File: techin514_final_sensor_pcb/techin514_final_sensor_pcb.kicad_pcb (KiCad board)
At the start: 2 copper layers, 7 parts, among them J2 J_BAT, J4 J_LDO, J6 J_IMU, J7 J_PWR

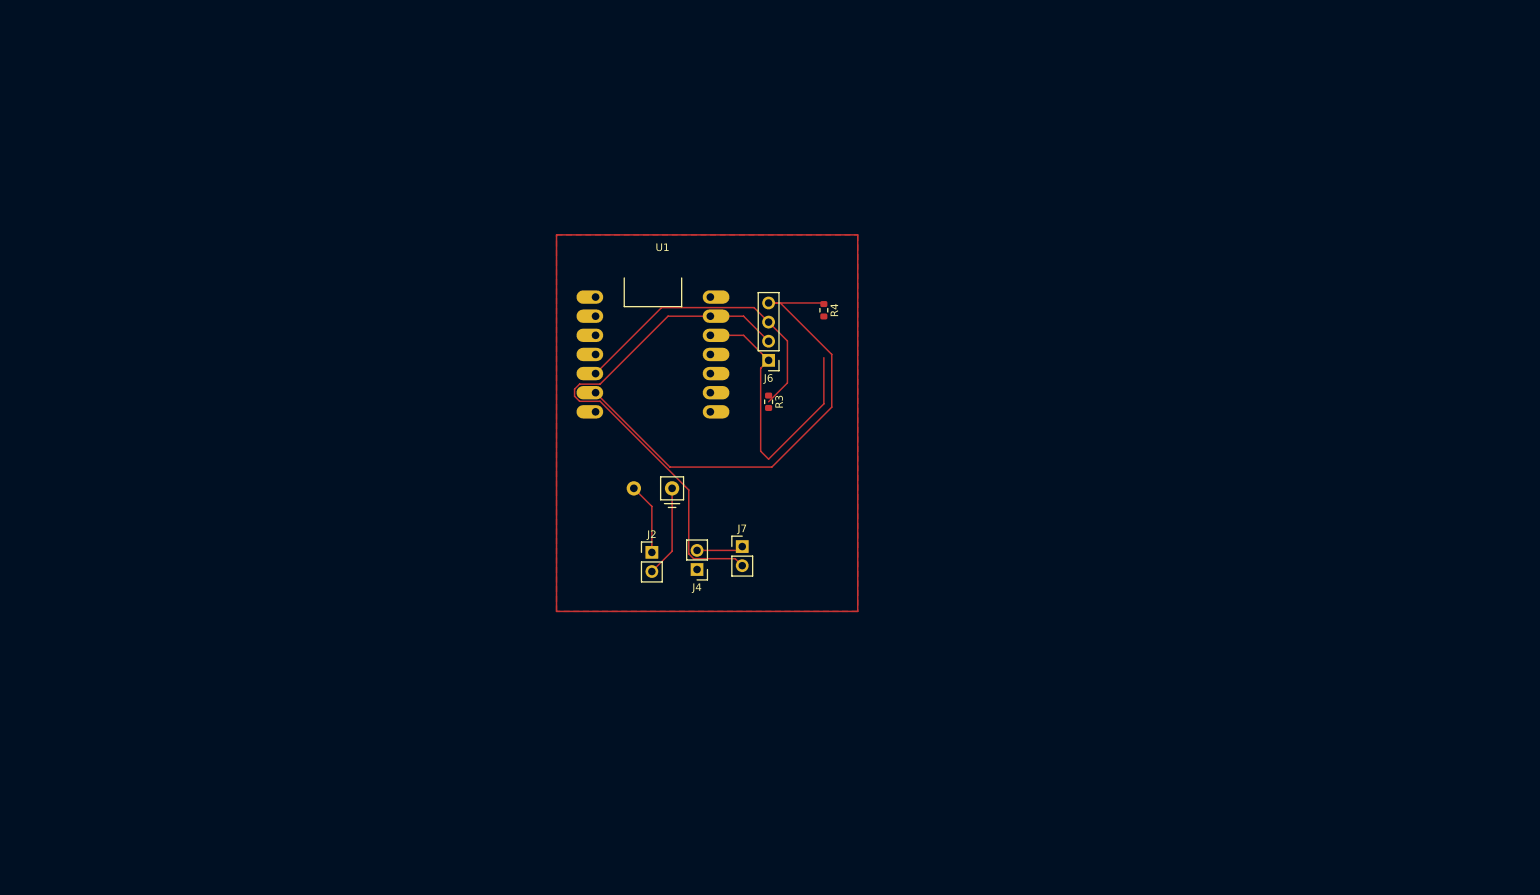
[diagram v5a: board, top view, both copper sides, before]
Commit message: update ble
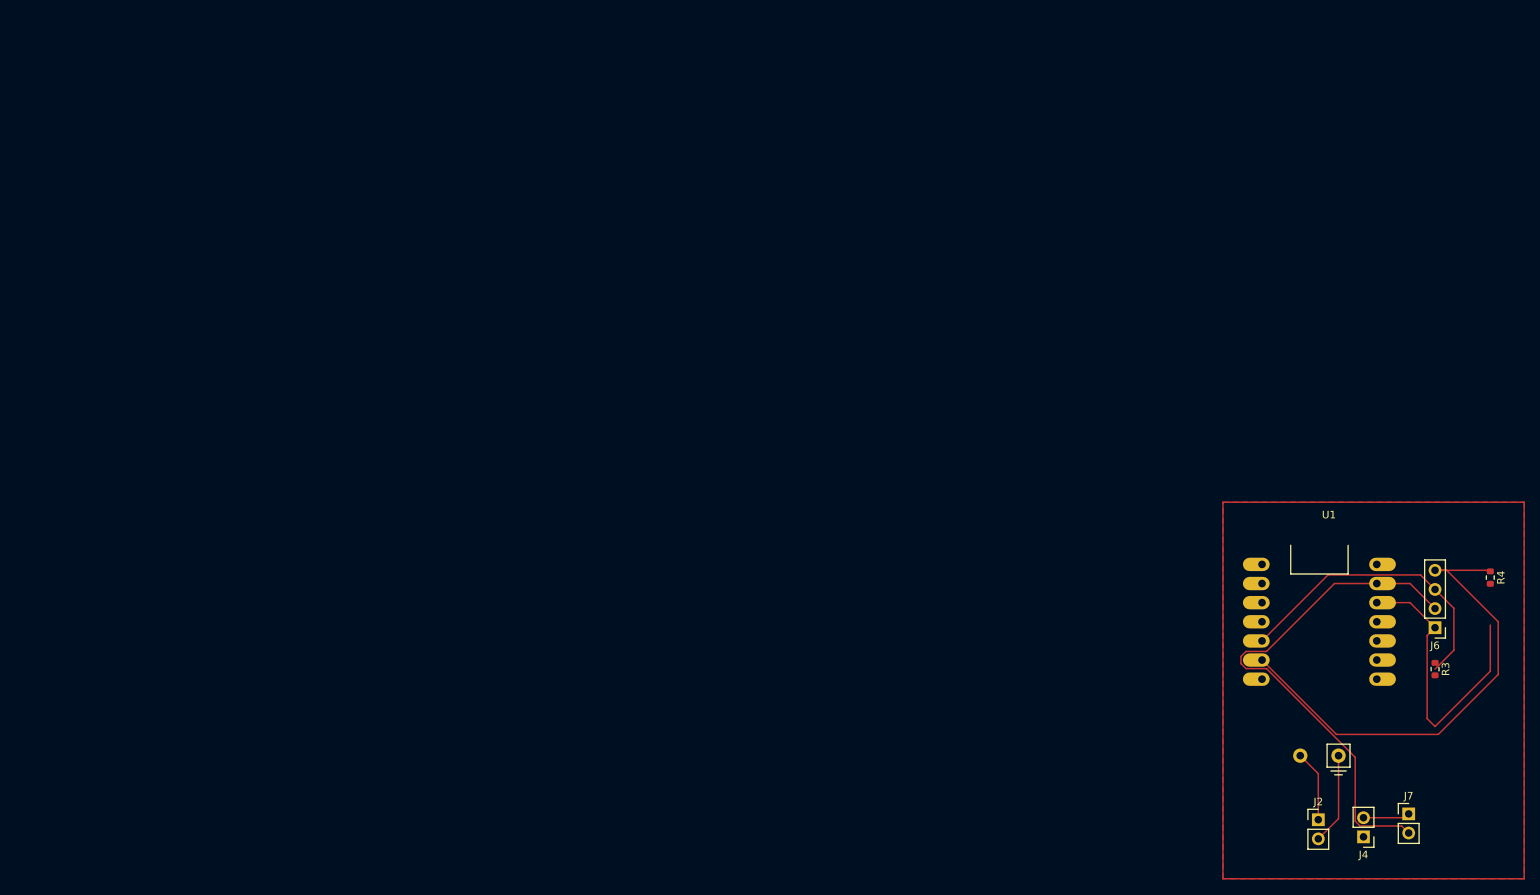
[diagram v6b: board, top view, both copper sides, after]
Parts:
- moved J2 95.4 mm to (223.1, 151.3)
- moved J4 95.4 mm to (229.1, 153.6)
- moved J6 95.4 mm to (238.6, 125.8)
- moved J7 95.4 mm to (235.1, 150.6)
- moved R3 95.4 mm to (238.6, 131.3)
- moved R4 95.4 mm to (245.9, 119.2)
- moved U1 95.4 mm to (223.2, 125.0)
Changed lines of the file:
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@@
 	(paper "A4")
 	(title_block
-		(title "Pet Activity & Proximity Tracker")
+		(title "Pet Activity & Proximity Tracker(Sensor PCB)")
 		(date "2026-02-04")
 		(rev "v0.1(draft)")
@@
 	(footprint "Connector_PinHeader_2.54mm:PinHeader_1x02_P2.54mm_Vertical"
 		(layer "F.Cu")
-		(at 140.564661 118.104 180)
+		(at 229.064661 153.604 180)
 		(descr "Through hole straight pin header, 1x02, 2.54mm pitch, single row")
 		(tags "Through hole pin header THT 1x02 2.54mm single row")
@@
 	(footprint "Connector_PinHeader_2.54mm:PinHeader_1x02_P2.54mm_Vertical"
 		(layer "F.Cu")
-		(at 146.564661 115.054)
+		(at 235.064661 150.554)
 		(descr "Through hole straight pin header, 1x02, 2.54mm pitch, single row")
 		(tags "Through hole pin header THT 1x02 2.54mm single row")
@@
 	(footprint "Resistor_SMD:R_0603_1608Metric"
 		(layer "F.Cu")
-		(at 157.402161 83.675 -90)
+		(at 245.902161 119.175 -90)
 		(descr "Resistor SMD 0603 (1608 Metric), square (rectangular) end terminal, IPC-7351 nominal, (Body size source: IPC-SM-782 page 72, https://www.pcb-3d.com/wordpress/wp-content/uploads/ipc-sm-782a_amendment_1_and_2.pdf), generated with kicad-footprint-generator")
 		(tags "resistor")
@@
 	(footprint "Resistor_SMD:R_0603_1608Metric"
 		(layer "F.Cu")
-		(at 150.064661 95.829 -90)
+		(at 238.564661 131.329 -90)
 		(descr "Resistor SMD 0603 (1608 Metric), square (rectangular) end terminal, IPC-7351 nominal, (Body size source: IPC-SM-782 page 72, https://www.pcb-3d.com/wordpress/wp-content/uploads/ipc-sm-782a_amendment_1_and_2.pdf), generated with kicad-footprint-generator")
 		(tags "resistor")
@@
 	(footprint "ESP32footprint:XIAO_ESP32"
 		(layer "F.Cu")
-		(at 134.709661 89.544)
+		(at 223.209661 125.044)
 		(property "Reference" "U1"
 			(at 1.27 -14.2 0)
@@
 	(footprint "Connector_PinHeader_2.54mm:PinHeader_1x04_P2.54mm_Vertical"
 		(layer "F.Cu")
-		(at 150.064661 90.329 180)
+		(at 238.564661 125.829 180)
 		(descr "Through hole straight pin header, 1x04, 2.54mm pitch, single row")
 		(tags "Through hole pin header THT 1x04 2.54mm single row")
@@
 	(footprint "Connector_PinHeader_2.54mm:PinHeader_1x02_P2.54mm_Vertical"
 		(layer "F.Cu")
-		(at 134.564661 115.829)
+		(at 223.064661 151.329)
 		(descr "Through hole straight pin header, 1x02, 2.54mm pitch, single row")
 		(tags "Through hole pin header THT 1x02 2.54mm single row")
@@
 	)
 	(gr_rect
-		(start 121.902161 73.6665)
-		(end 161.902161 123.6665)
+		(start 210.402161 109.1665)
+		(end 250.402161 159.1665)
 		(stroke
 			(width 0.2)
@@
 	)
 	(segment
-		(start 134.564661 115.829)
-		(end 134.564661 109.719)
+		(start 223.064661 151.329)
+		(end 223.064661 145.219)
 		(width 0.2)
 		(layer "F.Cu")
@@
 	)
 	(segment
-		(start 134.564661 109.719)
-		(end 132.169661 107.324)
+		(start 223.064661 145.219)
+		(end 220.669661 142.824)
 		(width 0.2)
 		(layer "F.Cu")
@@
 	)
 	(segment
-		(start 134.564661 118.369)
-		(end 137.249661 115.684)
+		(start 223.064661 153.869)
+		(end 225.749661 151.184)
 		(width 0.2)
 		(layer "F.Cu")
@@
 	)
 	(segment
-		(start 137.249661 115.684)
-		(end 137.249661 107.324)
+		(start 225.749661 151.184)
+		(end 225.749661 142.824)
 		(width 0.2)
 		(layer "F.Cu")
@@
 	)
 	(segment
-		(start 157.402161 96.1115)
-		(end 150.064661 103.449)
+		(start 245.902161 131.6115)
+		(end 238.564661 138.949)
 		(width 0.2)
 		(layer "F.Cu")
@@
 	)
 	(segment
-		(start 142.329661 87.004)
-		(end 146.739661 87.004)
+		(start 230.829661 122.504)
+		(end 235.239661 122.504)
 		(width 0.2)
 		(layer "F.Cu")
@@
 	)
 	(segment
-		(start 146.739661 87.004)
-		(end 150.064661 90.329)
+		(start 235.239661 122.504)
+		(end 238.564661 125.829)
 		(width 0.2)
 		(layer "F.Cu")
@@
 	)
 	(segment
-		(start 149.013661 102.398)
-		(end 149.013661 91.38)
+		(start 237.513661 137.898)
+		(end 237.513661 126.88)
 		(width 0.2)
 		(layer "F.Cu")
@@
 	)
 	(segment
-		(start 150.064661 103.449)
-		(end 149.013661 102.398)
+		(start 238.564661 138.949)
+		(end 237.513661 137.898)
 		(width 0.2)
 		(layer "F.Cu")
@@
 	)
 	(segment
-		(start 140.564661 115.564)
-		(end 146.054661 115.564)
+		(start 229.064661 151.064)
+		(end 234.554661 151.064)
 		(width 0.2)
 		(layer "F.Cu")
@@
 	)
 	(segment
-		(start 146.054661 115.564)
-		(end 146.564661 115.054)
+		(start 234.554661 151.064)
+		(end 235.064661 150.554)
 		(width 0.2)
 		(layer "F.Cu")
@@
 	)
 	(segment
-		(start 149.013661 91.38)
-		(end 150.064661 90.329)
+		(start 237.513661 126.88)
+		(end 238.564661 125.829)
 		(width 0.2)
 		(layer "F.Cu")
@@
 	)
 	(segment
-		(start 157.402161 89.9765)
-		(end 157.402161 96.1115)
+		(start 245.902161 125.4765)
+		(end 245.902161 131.6115)
 		(width 0.2)
 		(layer "F.Cu")
@@
 	)
 	(segment
-		(start 157.261161 82.709)
-		(end 157.402161 82.85)
+		(start 245.761161 118.209)
+		(end 245.902161 118.35)
 		(width 0.2)
 		(layer "F.Cu")
@@
 	)
 	(segment
-		(start 150.064661 82.709)
-		(end 151.621 82.709)
+		(start 238.564661 118.209)
+		(end 240.121 118.209)
 		(width 0.2)
 		(layer "F.Cu")
@@
 	)
 	(segment
-		(start 158.453161 96.546839)
-		(end 150.5 104.5)
+		(start 246.953161 132.046839)
+		(end 239 140)
 		(width 0.2)
 		(layer "F.Cu")
@@
 	)
 	(segment
-		(start 150.064661 82.709)
-		(end 157.261161 82.709)
+		(start 238.564661 118.209)
+		(end 245.761161 118.209)
 		(width 0.2)
 		(layer "F.Cu")
@@
 	)
 	(segment
-		(start 150.5 104.5)
-		(end 136.965661 104.5)
+		(start 239 140)
+		(end 225.465661 140)
 		(width 0.2)
 		(layer "F.Cu")
@@
 	)
 	(segment
-		(start 151.621 82.709)
-		(end 158.453161 89.541161)
+		(start 240.121 118.209)
+		(end 246.953161 125.041161)
 		(width 0.2)
 		(layer "F.Cu")
@@
 	)
 	(segment
-		(start 136.965661 104.5)
-		(end 127.089661 94.624)
+		(start 225.465661 140)
+		(end 215.589661 130.124)
 		(width 0.2)
 		(layer "F.Cu")
@@
 	)
 	(segment
-		(start 158.453161 89.541161)
-		(end 158.453161 96.546839)
+		(start 246.953161 125.041161)
+		(end 246.953161 132.046839)
 		(width 0.2)
 		(layer "F.Cu")
@@
 	)
 	(segment
-		(start 124.298661 95.096203)
-		(end 124.298661 94.151797)
+		(start 212.798661 130.596203)
+		(end 212.798661 129.651797)
 		(width 0.2)
 		(layer "F.Cu")
@@
 	)
 	(segment
-		(start 124.966458 95.764)
-		(end 124.298661 95.096203)
+		(start 213.466458 131.264)
+		(end 212.798661 130.596203)
 		(width 0.2)
 		(layer "F.Cu")
@@
 	)
 	(segment
-		(start 140.108611 116.665)
-		(end 139.463661 116.02005)
+		(start 228.608611 152.165)
+		(end 227.963661 151.52005)
 		(width 0.2)
 		(layer "F.Cu")
@@
 	)
 	(segment
-		(start 127.688864 93.484)
-		(end 136.708864 84.464)
+		(start 216.188864 128.984)
+		(end 225.208864 119.964)
 		(width 0.2)
 		(layer "F.Cu")
@@
 	)
 	(segment
-		(start 127.688864 95.764)
-		(end 124.966458 95.764)
+		(start 216.188864 131.264)
+		(end 213.466458 131.264)
 		(width 0.2)
 		(layer "F.Cu")
@@
 	)
 	(segment
-		(start 124.966458 93.484)
-		(end 127.688864 93.484)
+		(start 213.466458 128.984)
+		(end 216.188864 128.984)
 		(width 0.2)
 		(layer "F.Cu")
@@
 	)
 	(segment
-		(start 124.298661 94.151797)
-		(end 124.966458 93.484)
+		(start 212.798661 129.651797)
+		(end 213.466458 128.984)
 		(width 0.2)
 		(layer "F.Cu")
@@
 	)
 	(segment
-		(start 142.329661 84.464)
-		(end 146.739661 84.464)
+		(start 230.829661 119.964)
+		(end 235.239661 119.964)
 		(width 0.2)
 		(layer "F.Cu")
@@
 	)
 	(segment
-		(start 145.635661 116.665)
-		(end 140.108611 116.665)
+		(start 234.135661 152.165)
+		(end 228.608611 152.165)
 		(width 0.2)
 		(layer "F.Cu")
@@
 	)
 	(segment
-		(start 146.739661 84.464)
-		(end 150.064661 87.789)
+		(start 235.239661 119.964)
+		(end 238.564661 123.289)
 		(width 0.2)
 		(layer "F.Cu")
@@
 	)
 	(segment
-		(start 139.463661 116.02005)
-		(end 139.463661 107.538797)
+		(start 227.963661 151.52005)
+		(end 227.963661 143.038797)
 		(width 0.2)
 		(layer "F.Cu")
@@
 	)
 	(segment
-		(start 146.564661 117.594)
-		(end 145.635661 116.665)
+		(start 235.064661 153.094)
+		(end 234.135661 152.165)
 		(width 0.2)
 		(layer "F.Cu")
@@
 	)
 	(segment
-		(start 136.708864 84.464)
-		(end 142.329661 84.464)
+		(start 225.208864 119.964)
+		(end 230.829661 119.964)
 		(width 0.2)
 		(layer "F.Cu")
@@
 	)
 	(segment
-		(start 139.463661 107.538797)
-		(end 127.688864 95.764)
+		(start 227.963661 143.038797)
+		(end 216.188864 131.264)
 		(width 0.2)
 		(layer "F.Cu")
@@
 	)
 	(segment
-		(start 152.564661 87.749)
-		(end 150.064661 85.249)
+		(start 241.064661 123.249)
+		(end 238.564661 120.749)
 		(width 0.2)
 		(layer "F.Cu")
@@
 	)
 	(segment
-		(start 150.064661 85.249)
-		(end 148.139661 83.324)
+		(start 238.564661 120.749)
+		(end 236.639661 118.824)
 		(width 0.2)
 		(layer "F.Cu")
@@
 	)
 	(segment
-		(start 135.849661 83.324)
-		(end 127.089661 92.084)
+		(start 224.349661 118.824)
+		(end 215.589661 127.584)
 		(width 0.2)
 		(layer "F.Cu")
@@
 	)
 	(segment
-		(start 126.724661 92.449)
-		(end 127.089661 92.084)
+		(start 215.224661 127.949)
+		(end 215.589661 127.584)
 		(width 0.2)
 		(layer "F.Cu")
@@
 	)
 	(segment
-		(start 152.564661 93.329)
-		(end 152.564661 87.749)
+		(start 241.064661 128.829)
+		(end 241.064661 123.249)
 		(width 0.2)
 		(layer "F.Cu")
@@
 	)
 	(segment
-		(start 148.139661 83.324)
-		(end 135.849661 83.324)
+		(start 236.639661 118.824)
+		(end 224.349661 118.824)
 		(width 0.2)
 		(layer "F.Cu")
@@
 	)
 	(segment
-		(start 150.064661 95.829)
-		(end 152.564661 93.329)
+		(start 238.564661 131.329)
+		(end 241.064661 128.829)
 		(width 0.2)
 		(layer "F.Cu")
@@
 		(polygon
 			(pts
-				(xy 121.902161 73.6665) (xy 161.902161 73.6665) (xy 161.902161 123.6665) (xy 121.902161 123.6665)
-			)
-		)
+				(xy 210.402161 109.1665) (xy 250.402161 109.1665) (xy 250.402161 159.1665) (xy 210.402161 159.1665)
+			)
+		)
